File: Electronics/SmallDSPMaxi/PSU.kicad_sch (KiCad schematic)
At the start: 37 parts, among them J4 B4P-VH, U6 LM317_TO-252, U7 LM317_TO-252

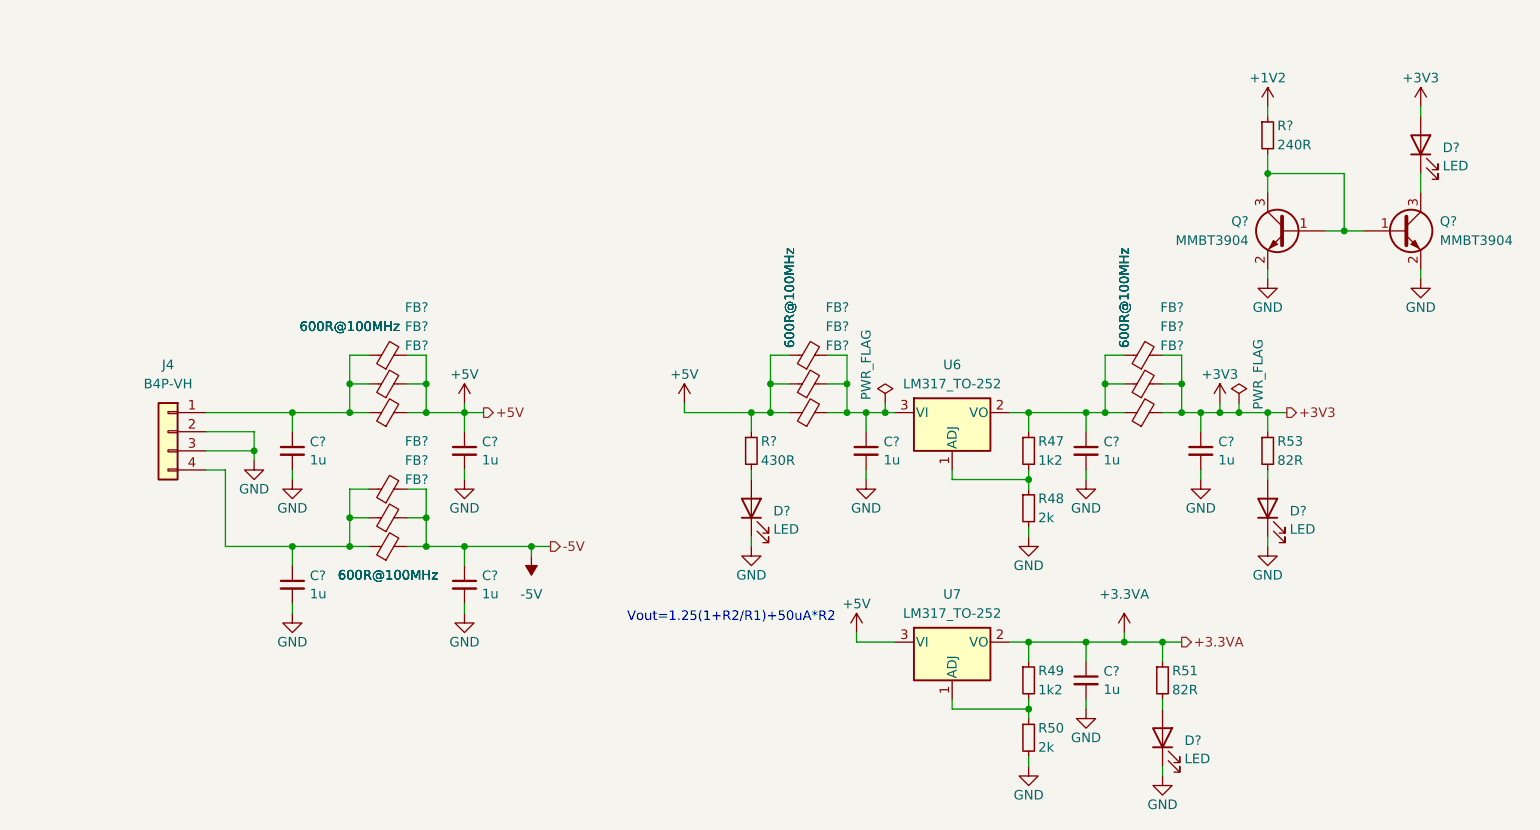
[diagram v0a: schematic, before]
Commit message: Finishes SmallDSP Maxi plus the fitting In- and Output Boards
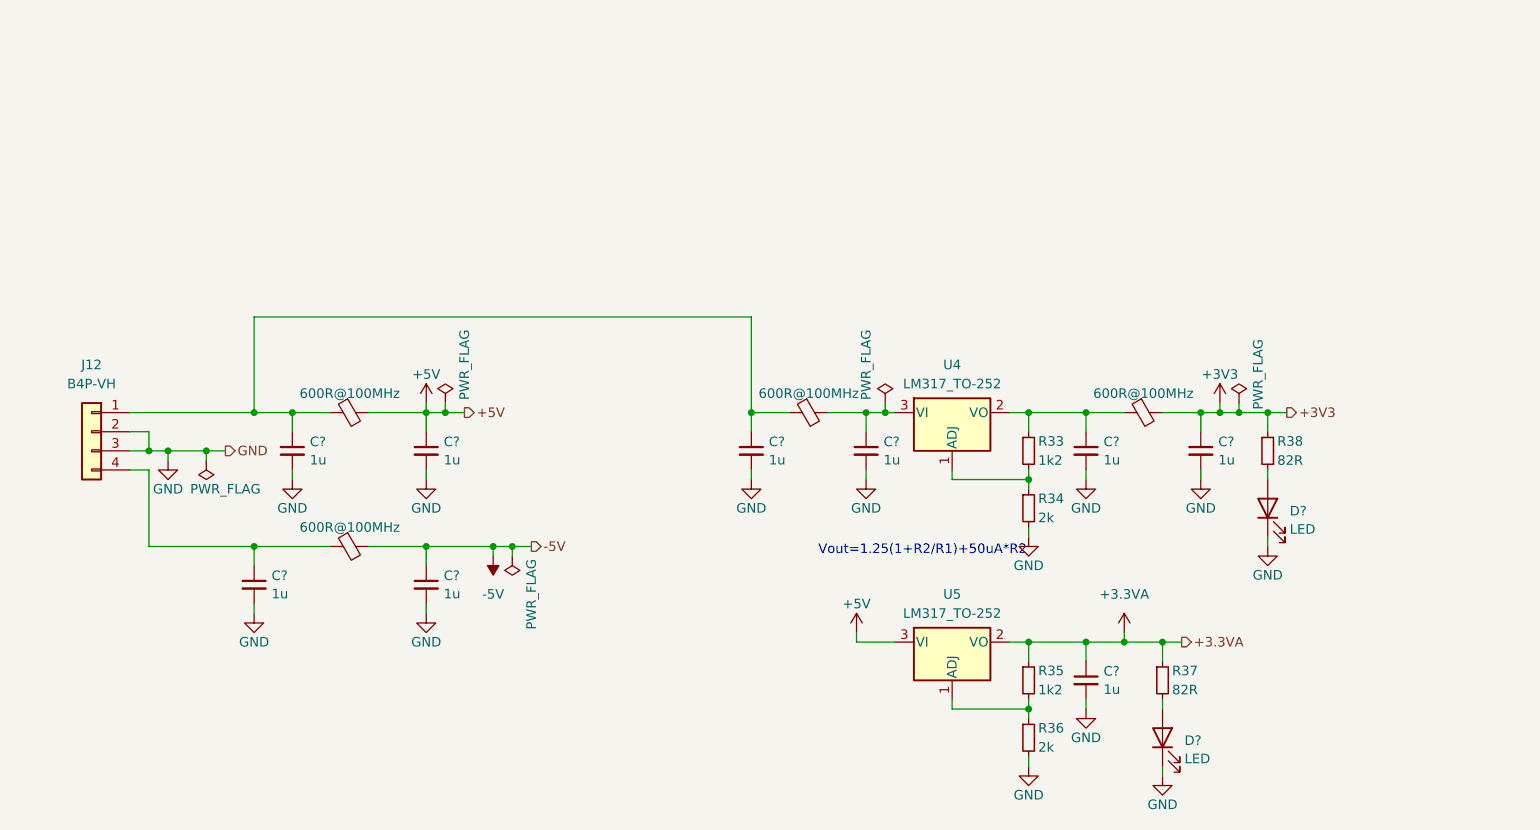
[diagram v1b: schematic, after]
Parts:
- removed D? (x2): LED, LED_SMD:LED_0603_1608Metric, symbol Device:LED
- removed FB? (x12): 600R@100MHz, Inductor_SMD:L_0805_2012Metric, symbol Device:FerriteBead_Small
- removed Q? (x2): MMBT3904, Package_TO_SOT_SMD:SOT-23, symbol Transistor_BJT:MMBT3904
- removed R?: 430R, Resistor_SMD:R_0603_1608Metric, symbol Device:R_Small
- removed R?: 240R, Resistor_SMD:R_0603_1608Metric, symbol Device:R_Small
- added C?: 1u, Capacitor_SMD:C_0805_2012Metric, symbol Device:C_Small
- added FB? (x4): 600R@100MHz, Inductor_SMD:L_0805_2012Metric, symbol Device:FerriteBead_Small
- C? (x8): JLC Part Number C28323 -> (none); LCSC Part # (none) -> C28323
- D? (x2): JLC Part Number C72041 -> (none); LCSC Part # (none) -> C72041
- J12: renamed from J4; LCSC Part # (none) -> -
- R33: renamed from R47; JLC Part Number C25862 -> (none); LCSC Part # (none) -> C25862
- R34: renamed from R48; JLC Part Number C22975 -> (none); LCSC Part # (none) -> C22975
- R35: renamed from R49; JLC Part Number C25862 -> (none); LCSC Part # (none) -> C25862
- R36: renamed from R50; JLC Part Number C22975 -> (none); LCSC Part # (none) -> C22975
- R37: renamed from R51; JLC Part Number C23255 -> (none); LCSC Part # (none) -> C23255
- R38: renamed from R53; JLC Part Number C23255 -> (none); LCSC Part # (none) -> C23255
- U4: renamed from U6; JLC Part Number C75510 -> (none); LCSC Part # (none) -> C75510
- U5: renamed from U7; JLC Part Number C75510 -> (none); LCSC Part # (none) -> C75510
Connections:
- net +3V3: now also FB?.2
- net +5V: now also FB?.2
- net -5V: now also FB?.2
- net GND: now also C?.2
- net at C?.1, R33.1, U4.2 (VO): now also FB?.1
- net at C?.1, J12.1 (Pin_1): now also C?.1, FB?.1, FB?.1
- net at C?.1, U4.3 (VI): now also FB?.2
- net at C?.1, J12.4 (Pin_4): now also FB?.1
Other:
- moved on the sheet: C?, J12

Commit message: replaces 12pin IDC out header with 14pin one because of better availability.
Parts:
- FB? (x4): LCSC Part # (none) -> -
- J12: Assembling X -> (none)
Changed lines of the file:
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@@
       (effects (font (size 1.27 1.27)) hide)
     )
-    (property "LCSC Part #" "" (at 113.03 114.3 0)
+    (property "LCSC Part #" "-" (at 113.03 114.3 0)
       (effects (font (size 1.27 1.27)) hide)
     )
@@
       (effects (font (size 1.27 1.27)) hide)
     )
-    (property "LCSC Part #" "" (at 173.99 96.52 0)
+    (property "LCSC Part #" "-" (at 173.99 96.52 0)
       (effects (font (size 1.27 1.27)) hide)
     )
@@
       (effects (font (size 1.27 1.27)) hide)
     )
-    (property "LCSC Part #" "" (at 113.03 96.52 0)
+    (property "LCSC Part #" "-" (at 113.03 96.52 0)
       (effects (font (size 1.27 1.27)) hide)
     )
@@
       (effects (font (size 1.27 1.27)) hide)
     )
-    (property "LCSC Part #" "" (at 218.44 96.52 0)
+    (property "LCSC Part #" "-" (at 218.44 96.52 0)
       (effects (font (size 1.27 1.27)) hide)
     )
@@
       (effects (font (size 1.27 1.27)) hide)
     )
-    (property "Assembling" "X" (at 78.74 99.06 0)
-      (effects (font (size 1.27 1.27)) hide)
-    )
+    (property "Assembling" "" (at 78.74 99.06 0)
+      (effects (font (size 1.27 1.27)) hide)
+    )

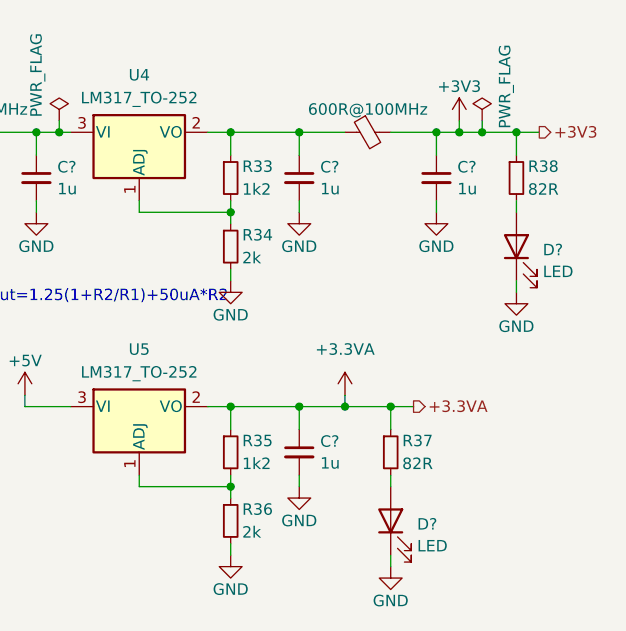
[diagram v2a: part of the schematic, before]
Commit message: Fixes schematic mistakes, like incorrect routin of clock to codecs
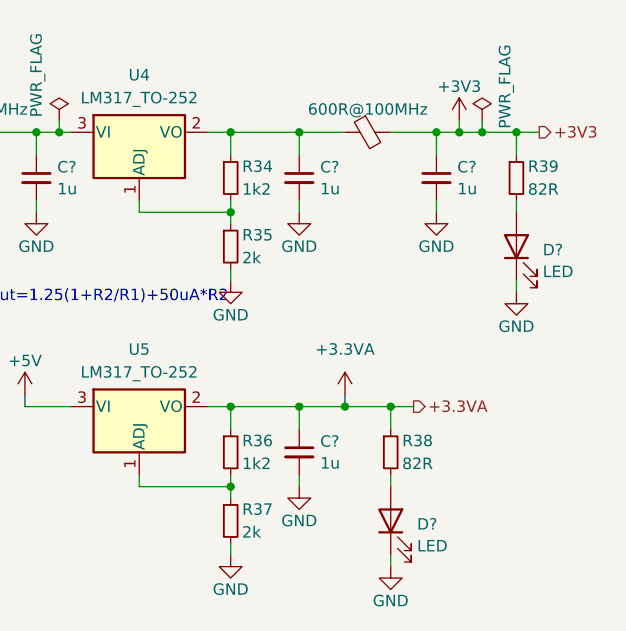
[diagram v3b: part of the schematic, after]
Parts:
- renumbered R33 to R34, R34 to R35, R35 to R36, R36 to R37, R37 to R38, R38 to R39

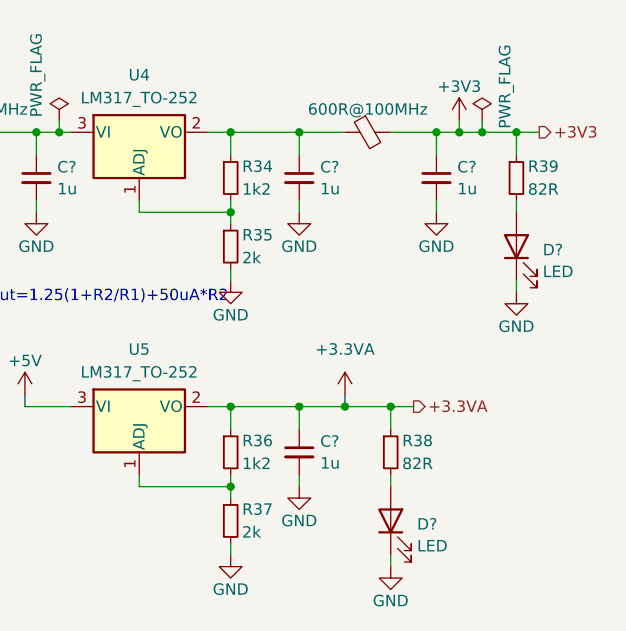
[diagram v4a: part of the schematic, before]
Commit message: Adds clock distributer
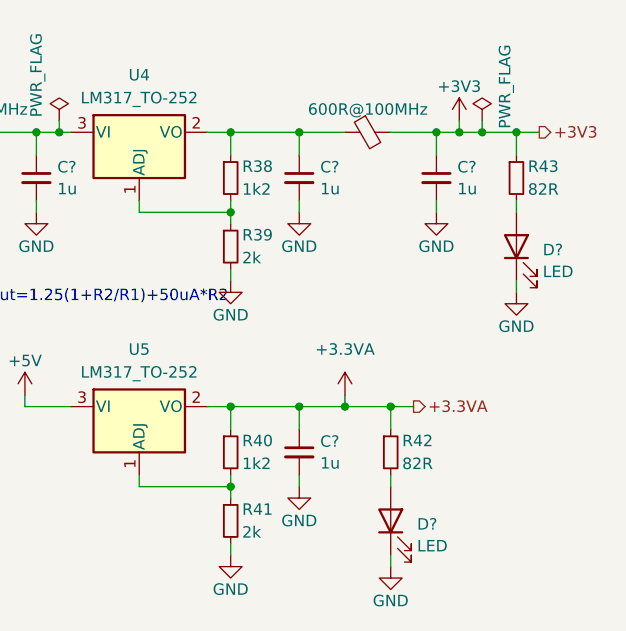
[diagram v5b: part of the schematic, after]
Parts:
- renumbered R34 to R38, R35 to R39, R36 to R40, R37 to R41, R38 to R42, R39 to R43
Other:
- title: SmallDSP -> SmallDSP Maxi

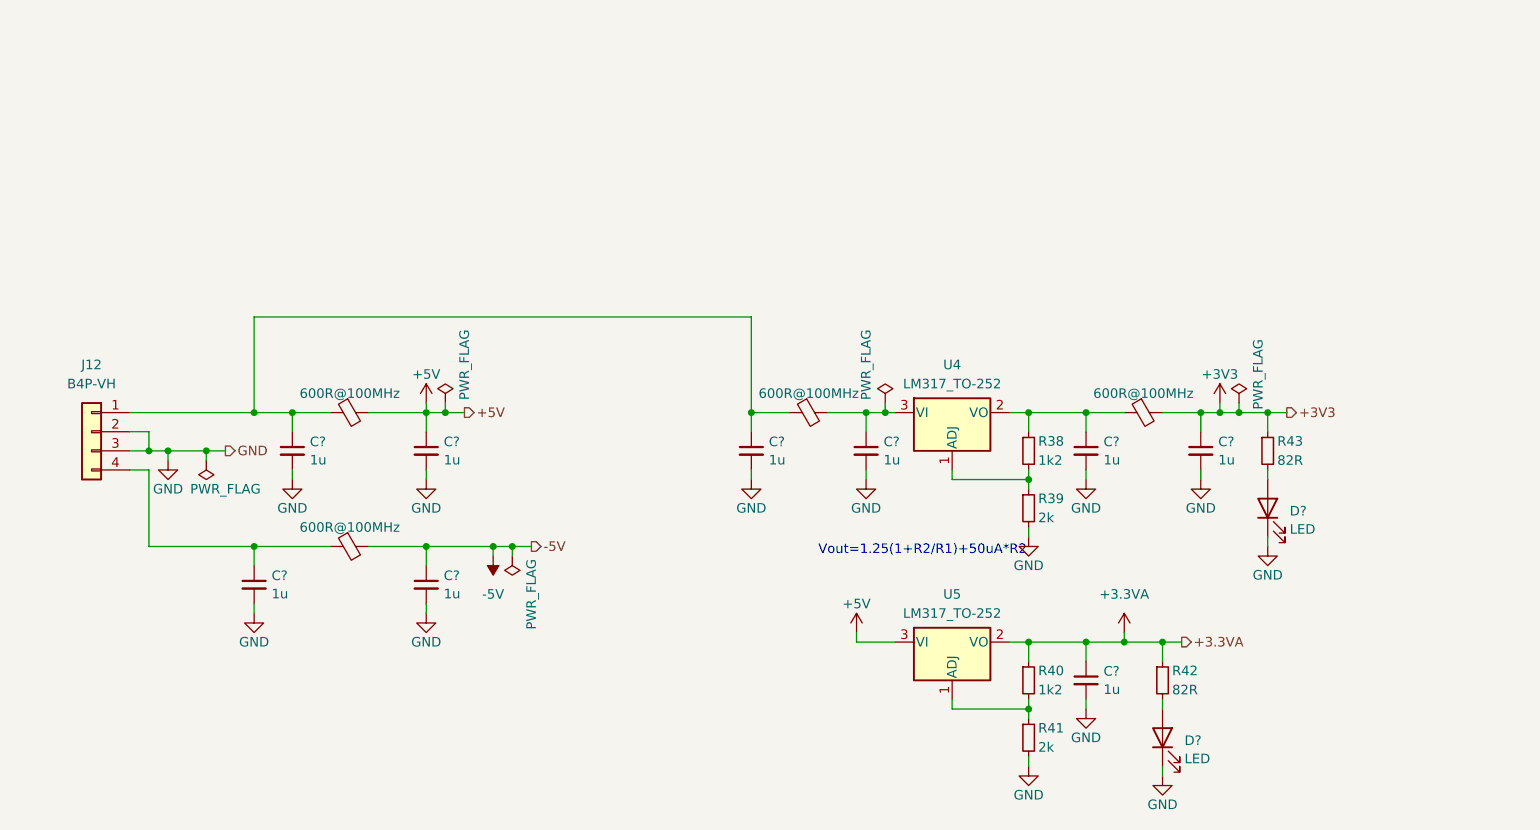
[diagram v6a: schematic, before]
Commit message: adds usb to i2s bridge to micro. Adds tweaks for layout of maxi.
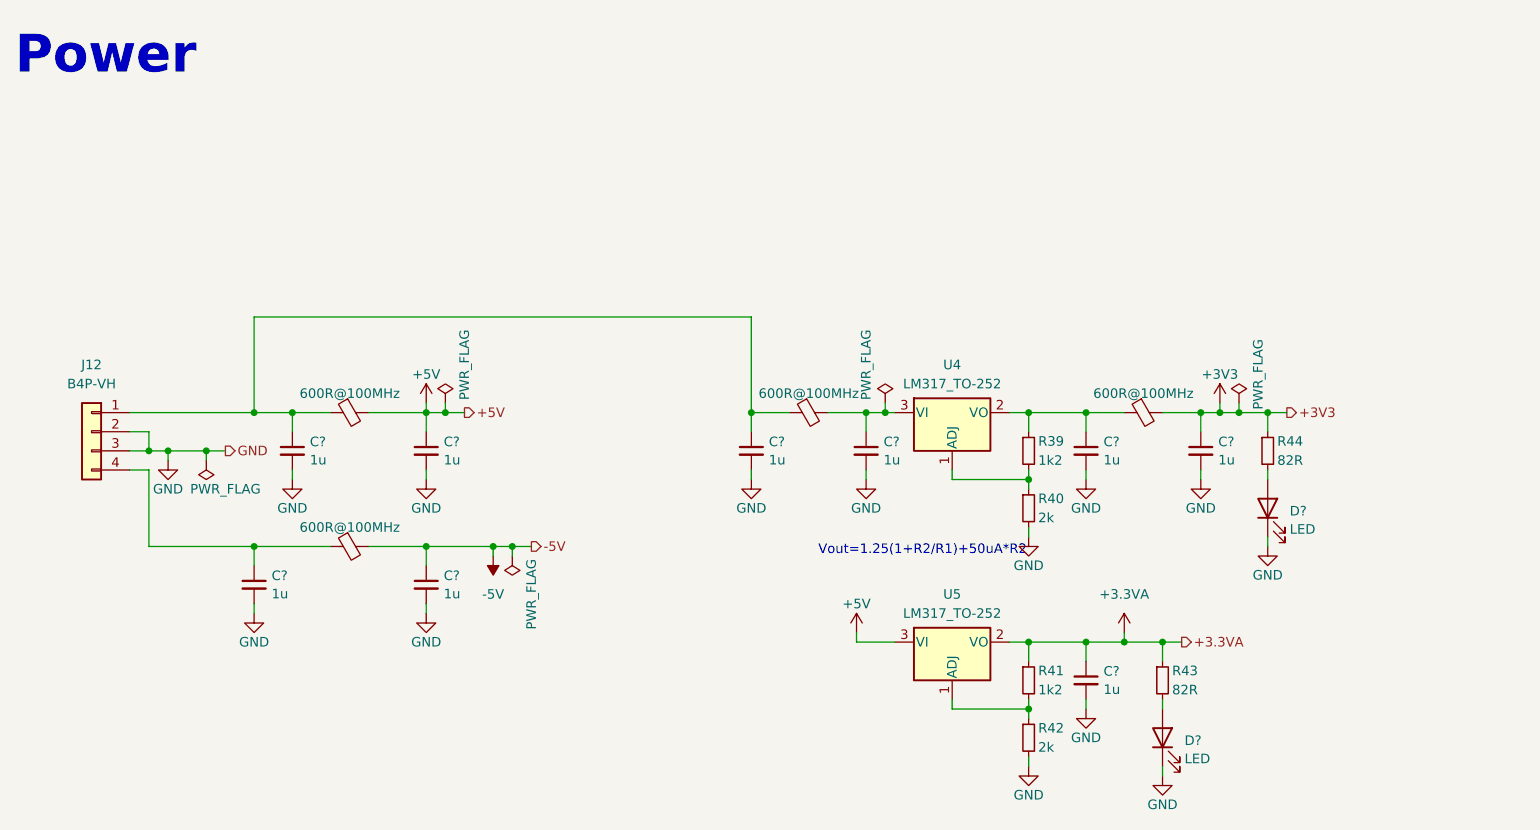
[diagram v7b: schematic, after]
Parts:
- U4, U5: footprint Package_TO_SOT_SMD:TO-252-2 -> 1_Project_Footprints:TO-252-2 thermal vias
- renumbered R38 to R39, R39 to R40, R40 to R41, R41 to R42, R42 to R43, R43 to R44
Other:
- note added: "Power"

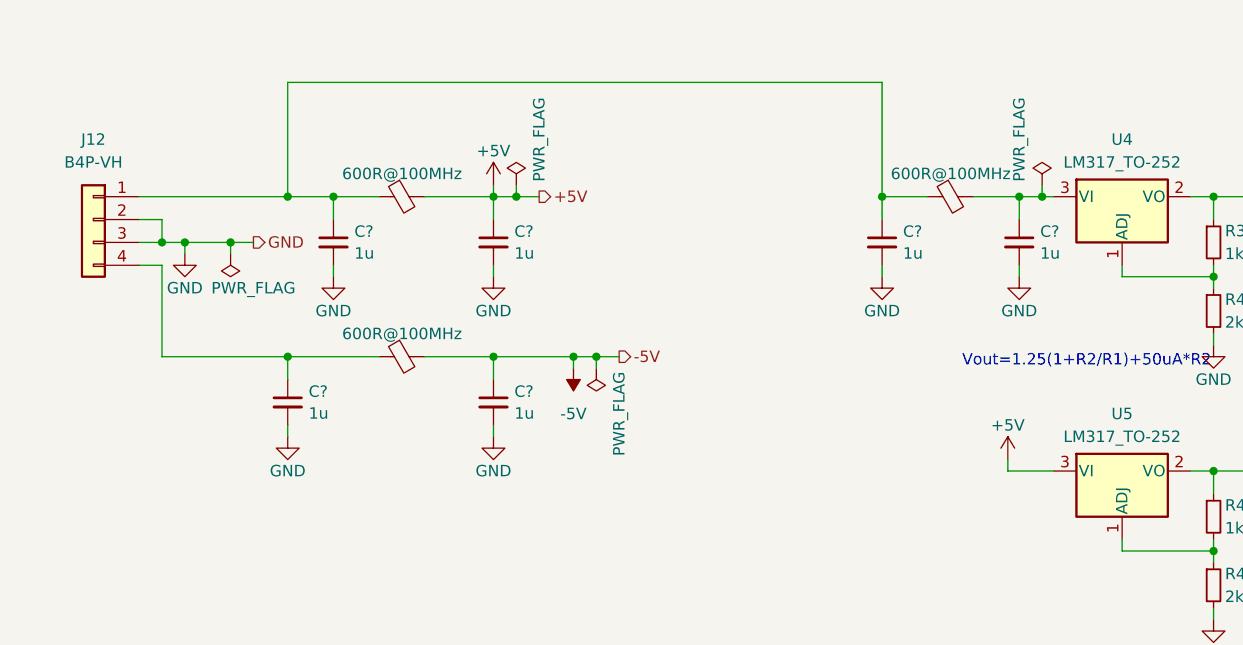
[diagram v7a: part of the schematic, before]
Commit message: Fixes wrong connection in maxi schematic
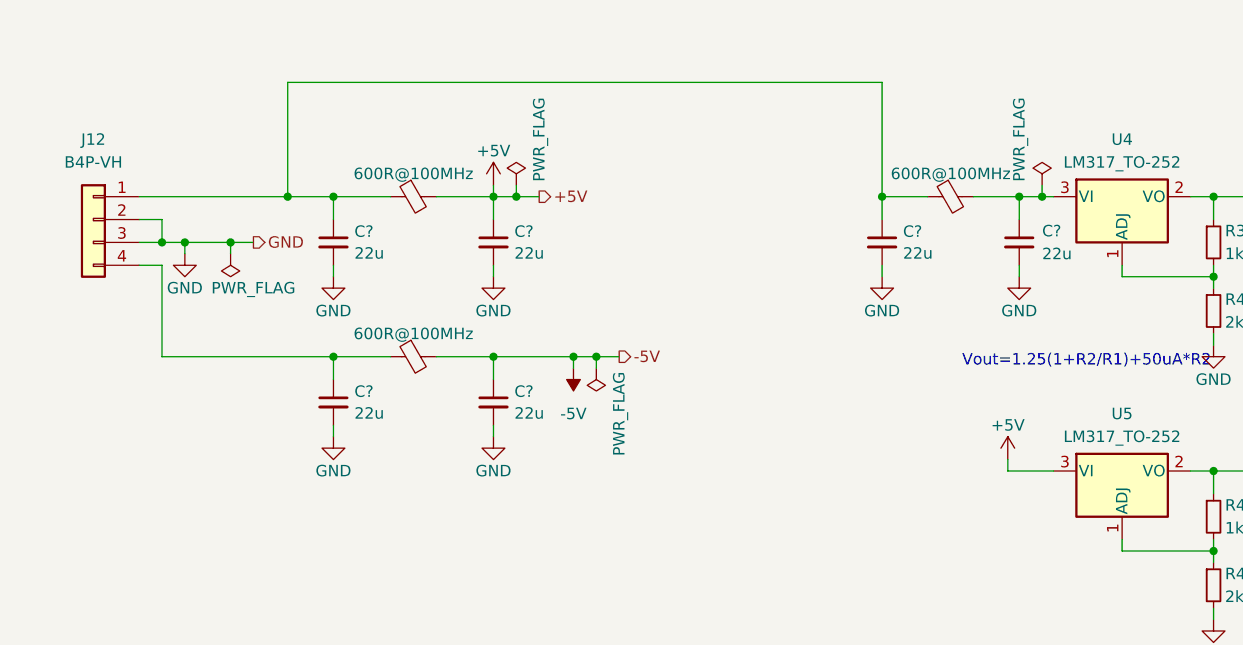
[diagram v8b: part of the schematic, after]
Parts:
- C? (x6): value 1u -> 22u; Dielectric X7R -> X5R; LCSC Part # C28323 -> C45783; Notes (none) -> -50%@5VDC; Part Number CL21B105KBFNNNE -> CL21A226MAQNNNE; Rated Voltage 50V -> 25V
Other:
- moved on the sheet: C?
